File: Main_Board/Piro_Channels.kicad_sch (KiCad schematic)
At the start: 0 parts

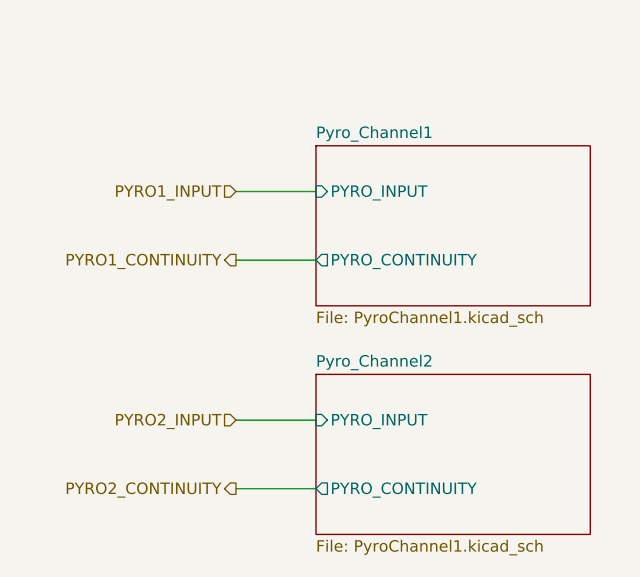
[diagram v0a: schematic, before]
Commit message: Schematic cleanup, ALED footprint + 3D + sch
+ layout and routing
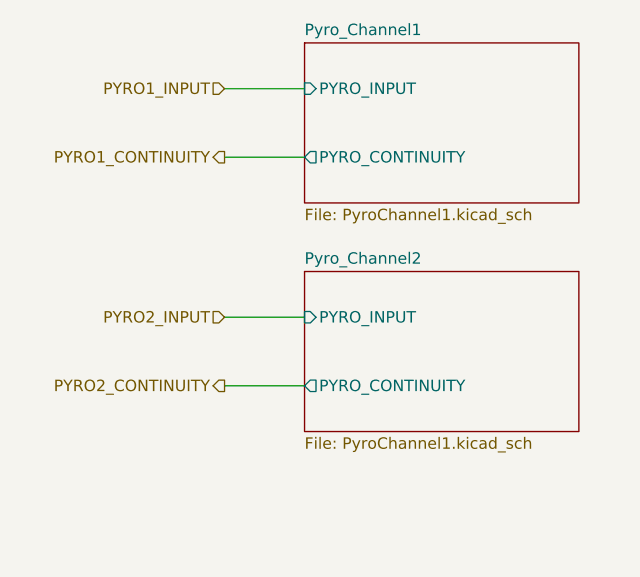
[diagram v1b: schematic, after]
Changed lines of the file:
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@@
 	(wire
 		(pts
-			(xy 129.54 120.65) (xy 138.43 120.65)
+			(xy 128.27 109.22) (xy 137.16 109.22)
 		)
 		(stroke
@@
 	(wire
 		(pts
-			(xy 129.54 128.27) (xy 138.43 128.27)
+			(xy 128.27 116.84) (xy 137.16 116.84)
 		)
 		(stroke
@@
 	(wire
 		(pts
-			(xy 129.54 95.25) (xy 138.43 95.25)
+			(xy 128.27 83.82) (xy 137.16 83.82)
 		)
 		(stroke
@@
 	(wire
 		(pts
-			(xy 129.54 102.87) (xy 138.43 102.87)
+			(xy 128.27 91.44) (xy 137.16 91.44)
 		)
 		(stroke
@@
 	(hierarchical_label "PYRO2_INPUT"
 		(shape input)
-		(at 129.54 120.65 180)
+		(at 128.27 109.22 180)
 		(effects
 			(font
@@
 	(hierarchical_label "PYRO2_CONTINUITY"
 		(shape output)
-		(at 129.54 128.27 180)
+		(at 128.27 116.84 180)
 		(effects
 			(font
@@
 	(hierarchical_label "PYRO1_CONTINUITY"
 		(shape output)
-		(at 129.54 102.87 180)
+		(at 128.27 91.44 180)
 		(effects
 			(font
@@
 	(hierarchical_label "PYRO1_INPUT"
 		(shape input)
-		(at 129.54 95.25 180)
+		(at 128.27 83.82 180)
 		(effects
 			(font
@@
 	)
 	(sheet
-		(at 138.43 115.57)
+		(at 137.16 104.14)
 		(size 30.48 17.78)
 		(exclude_from_sim no)
@@
 		)
 		(property "Sheetname" "Pyro_Channel2"
-			(at 138.43 114.8584 0)
+			(at 137.16 103.4284 0)
 			(show_name no)
 			(do_not_autoplace no)
@@
 		)
 		(property "Sheetfile" "PyroChannel1.kicad_sch"
-			(at 138.43 133.9346 0)
+			(at 137.16 122.5046 0)
 			(show_name no)
 			(do_not_autoplace no)
@@
 		)
 		(pin "PYRO_INPUT" input
-			(at 138.43 120.65 180)
+			(at 137.16 109.22 180)
 			(effects
 				(font
@@
 		)
 		(pin "PYRO_CONTINUITY" output
-			(at 138.43 128.27 180)
+			(at 137.16 116.84 180)
 			(effects
 				(font
@@
 	)
 	(sheet
-		(at 138.43 90.17)
+		(at 137.16 78.74)
 		(size 30.48 17.78)
 		(exclude_from_sim no)
@@
 		)
 		(property "Sheetname" "Pyro_Channel1"
-			(at 138.43 89.4584 0)
+			(at 137.16 78.0284 0)
 			(show_name no)
 			(do_not_autoplace no)
@@
 		)
 		(property "Sheetfile" "PyroChannel1.kicad_sch"
-			(at 138.43 108.5346 0)
+			(at 137.16 97.1046 0)
 			(show_name no)
 			(do_not_autoplace no)
@@
 		)
 		(pin "PYRO_INPUT" input
-			(at 138.43 95.25 180)
+			(at 137.16 83.82 180)
 			(effects
 				(font
@@
 		)
 		(pin "PYRO_CONTINUITY" output
-			(at 138.43 102.87 180)
+			(at 137.16 91.44 180)
 			(effects
 				(font
